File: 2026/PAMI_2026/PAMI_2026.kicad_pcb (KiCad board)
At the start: 2 copper layers, 75 x 69 mm, 69 parts, among them IC1 Transfo 5V -> 3.3V, J1 USB-C_12pin, J10 RANGE, J11 RANGE, J12 22-03-5035, J13 Conn_01x02_Pin, J14 Conn_01x02_Pin, J15 Conn_01x02_Pin, J2 Screw_Terminal_01x02, J3 Stepper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

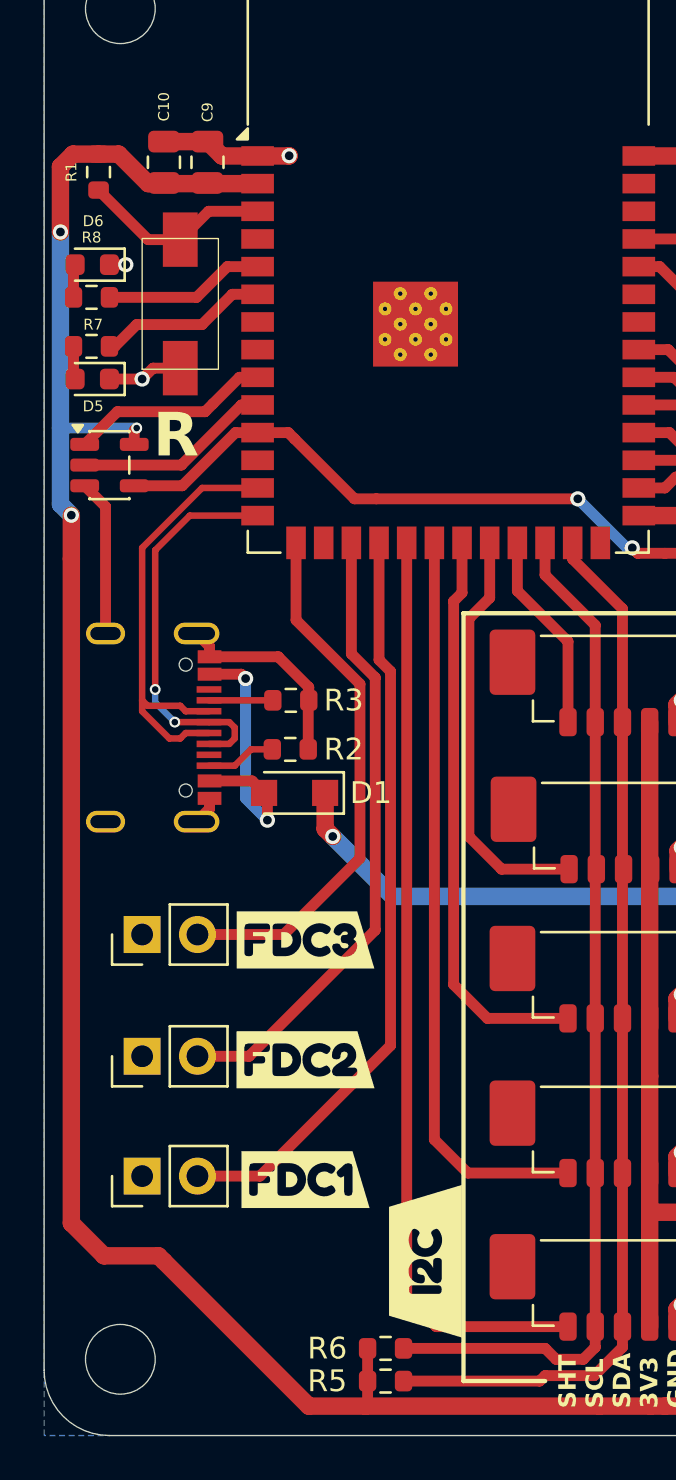
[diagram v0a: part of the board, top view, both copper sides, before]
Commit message: [PAMI 2026] Add IMU.
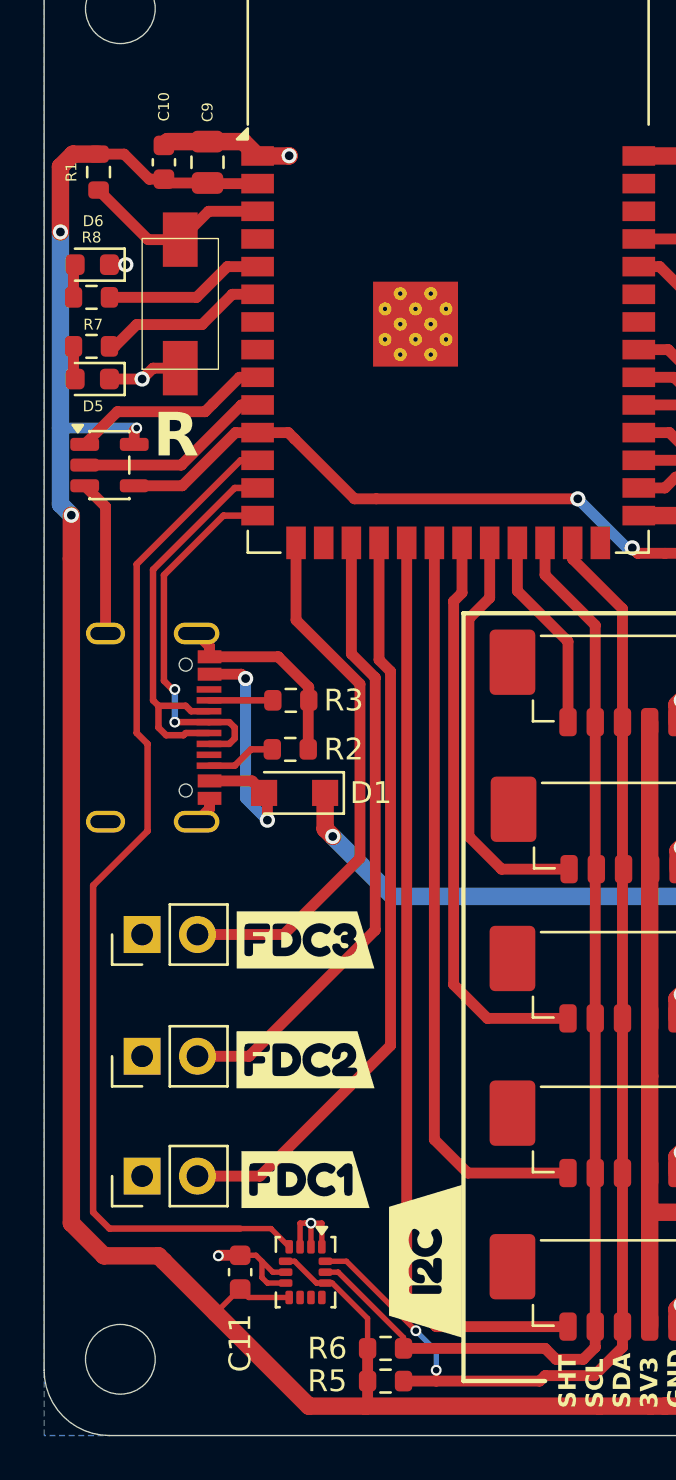
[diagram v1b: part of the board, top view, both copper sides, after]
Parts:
- added C11: 100nF, Capacitor_SMD:C_0603_1608Metric, F.Cu at (144.0, 104.0)
- added U4: LSM6DSL, Package_LGA:LGA-14_3x2.5mm_P0.5mm_LayoutBorder3x4y, F.Cu at (147.0, 104.0)
- C10: footprint Capacitor_SMD:C_0805_2012Metric -> Capacitor_SMD:C_0603_1608Metric
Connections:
- U1 pad 12: unconnected-(U1-IO8-Pad12) -> IMU_INT
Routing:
- net IMU_INT: track 0.00 -> 48.2 mm
- net +3.3V: track 264.5 -> 274.7 mm
- net GND: track 77.2 -> 86.9 mm, vias 19 -> 21
- net SDA: track 48.6 -> 56.7 mm, vias 0 -> 2
- net SCL: track 47.1 -> 52.4 mm
- net USB_DM: track 20.9 -> 18.6 mm
- net USB_DP: track 18.3 -> 17.1 mm
